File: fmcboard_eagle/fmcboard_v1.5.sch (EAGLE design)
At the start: 174 parts, among them IC1 OPA699ID, IC10 LTC6229IMS8E#TRPBF, IC11 7805TV, IC12 SN74AUC2G66DCTR, IC13 SN74AUC2G66DCTR, IC14 SN74AUC2G66DCTR, IC15 SN74AUC2G66DCTR, IC16 DAC7578SPWR, IC17 SN74AUC2G66DCTR, IC18 SN74AUC2G66DCTR, IC19 SN74AUC2G66DCTR, IC2 DAC7578SPWR, IC20 SN74AUC2G66DCTR, IC21 74LVC2GU04GV,125, IC22 74LVC2GU04GV,125, IC23 74LVC2GU04GV,125, IC24 74LVC2GU04GV,125, IC3 LTC6229IMS8E#TRPBF, IC4 LTC6229IMS8E#TRPBF, IC5 LM358, IC6 OPA699ID, IC7 OPA699ID, IC8 LTC6229IMS8E#TRPBF, IC9 LTC6229IMS8E#TRPBF, J1 8pin, J10 8pin, J12 4p-2.54, J2 ASP-134604-01, J3 4p-2.54, J4 4p-2.54, J5 8pin, J6 4p-2.54, J7 4p-2.54, J8 4p-2.54, J9 8pin, U1 TXS0108EPWR, U2 STMICROELECTRONICS_L7905ACVST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

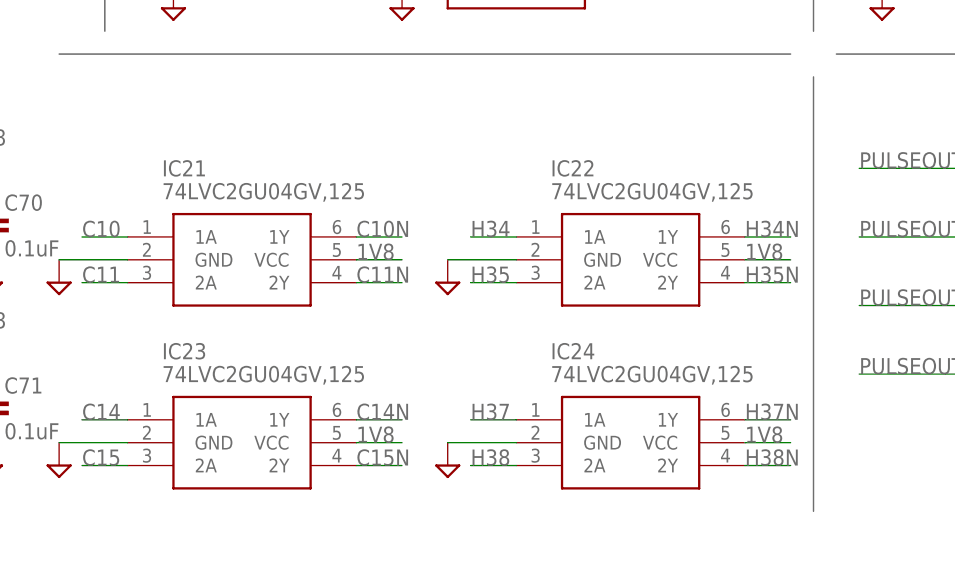
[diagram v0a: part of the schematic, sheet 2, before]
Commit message: Revert "Switch to 74LVC2GU04 inverters"
This reverts commit 0d5c0f9254668030431faa83bc2596f2b624104f.
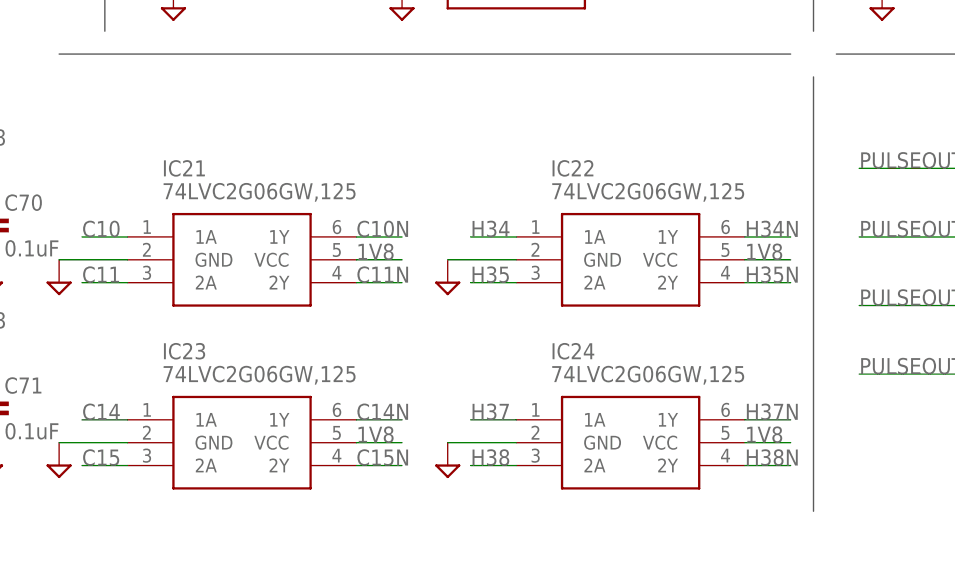
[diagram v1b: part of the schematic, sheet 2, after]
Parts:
- IC21, IC22, IC23, IC24: value 74LVC2GU04GV,125 -> 74LVC2G06GW,125; device 74LVC2GU04GV_125:74LVC2GU04GV,125 -> 74LVC2G06GW_125:74LVC2G06GW,125
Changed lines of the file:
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@@
 <part name="SUPPLY81" library="supply2" library_urn="urn:adsk.eagle:library:372" deviceset="GND" device=""/>
 <part name="SUPPLY82" library="supply2" library_urn="urn:adsk.eagle:library:372" deviceset="GND" device=""/>
-<part name="IC21" library="74LVC2GU04GV_125" deviceset="74LVC2GU04GV,125" device=""/>
-<part name="IC22" library="74LVC2GU04GV_125" deviceset="74LVC2GU04GV,125" device=""/>
-<part name="IC23" library="74LVC2GU04GV_125" deviceset="74LVC2GU04GV,125" device=""/>
-<part name="IC24" library="74LVC2GU04GV_125" deviceset="74LVC2GU04GV,125" device=""/>
+<part name="IC21" library="74LVC2G06GW_125" deviceset="74LVC2G06GW,125" device=""/>
+<part name="IC22" library="74LVC2G06GW_125" deviceset="74LVC2G06GW,125" device=""/>
+<part name="IC23" library="74LVC2G06GW_125" deviceset="74LVC2G06GW,125" device=""/>
+<part name="IC24" library="74LVC2G06GW_125" deviceset="74LVC2G06GW,125" device=""/>
 <part name="SUPPLY83" library="supply2" library_urn="urn:adsk.eagle:library:372" deviceset="GND" device=""/>
 <part name="SUPPLY84" library="supply2" library_urn="urn:adsk.eagle:library:372" deviceset="GND" device=""/>

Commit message: Switch to 74LVC2GU04 inverters
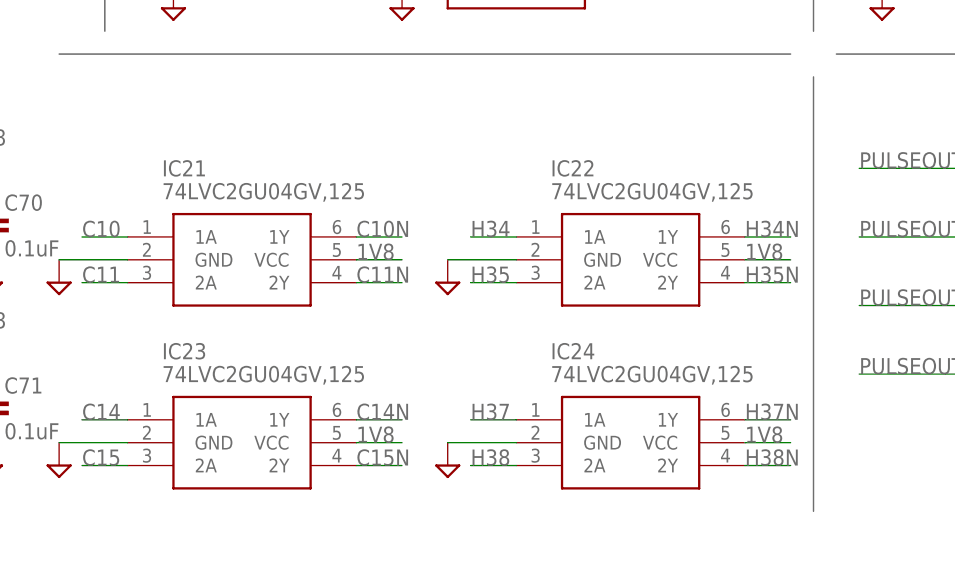
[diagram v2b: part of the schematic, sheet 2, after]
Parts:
- IC21, IC22, IC23, IC24: value 74LVC2G06GW,125 -> 74LVC2GU04GV,125; device 74LVC2G06GW_125:74LVC2G06GW,125 -> 74LVC2GU04GV_125:74LVC2GU04GV,125
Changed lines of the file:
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@@
 <part name="SUPPLY81" library="supply2" library_urn="urn:adsk.eagle:library:372" deviceset="GND" device=""/>
 <part name="SUPPLY82" library="supply2" library_urn="urn:adsk.eagle:library:372" deviceset="GND" device=""/>
-<part name="IC21" library="74LVC2G06GW_125" deviceset="74LVC2G06GW,125" device=""/>
-<part name="IC22" library="74LVC2G06GW_125" deviceset="74LVC2G06GW,125" device=""/>
-<part name="IC23" library="74LVC2G06GW_125" deviceset="74LVC2G06GW,125" device=""/>
-<part name="IC24" library="74LVC2G06GW_125" deviceset="74LVC2G06GW,125" device=""/>
+<part name="IC21" library="74LVC2GU04GV_125" deviceset="74LVC2GU04GV,125" device=""/>
+<part name="IC22" library="74LVC2GU04GV_125" deviceset="74LVC2GU04GV,125" device=""/>
+<part name="IC23" library="74LVC2GU04GV_125" deviceset="74LVC2GU04GV,125" device=""/>
+<part name="IC24" library="74LVC2GU04GV_125" deviceset="74LVC2GU04GV,125" device=""/>
 <part name="SUPPLY83" library="supply2" library_urn="urn:adsk.eagle:library:372" deviceset="GND" device=""/>
 <part name="SUPPLY84" library="supply2" library_urn="urn:adsk.eagle:library:372" deviceset="GND" device=""/>
